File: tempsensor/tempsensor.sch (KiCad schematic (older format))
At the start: 68 parts, among them J1 USB_B_Micro, Q1 BC817, Q2 BC817, Q3 BC817, SW1 SW_DIP_x06, SW2 PW_OFF, SW3 PW_ON, U1 PCF8574, U2 ESP-12F, U3 24C16, U4 MCP73831-2-OT, U5 MCP9844, U6 MAX17620

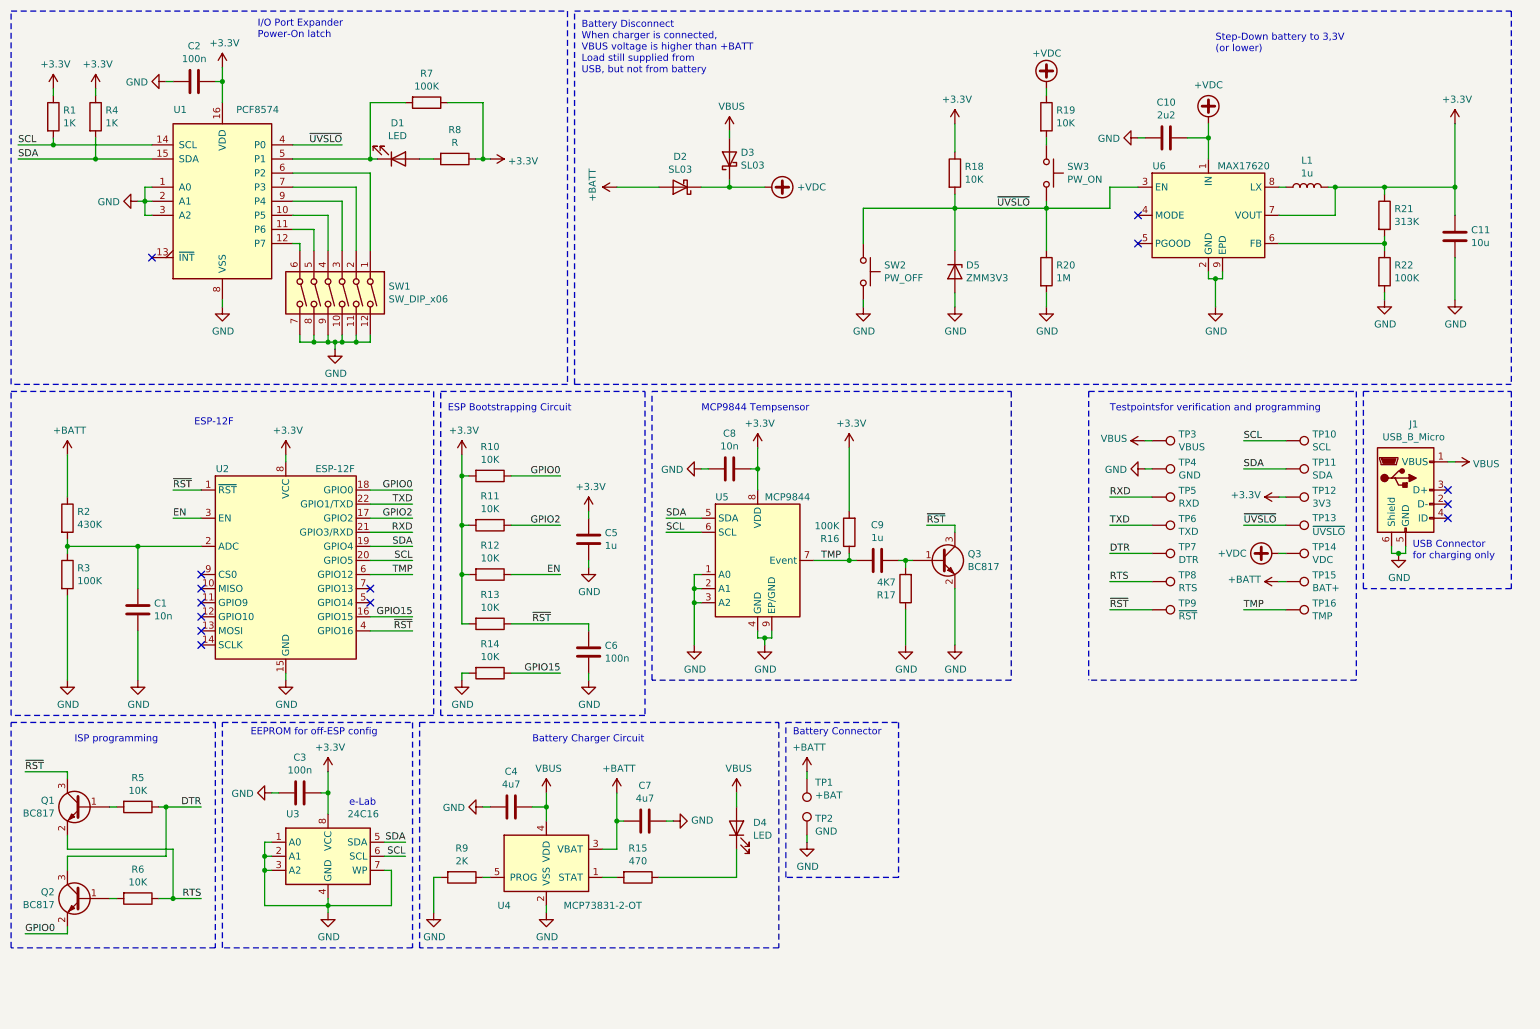
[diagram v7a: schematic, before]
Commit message: Created 4x4cm PCB for tempsensor, first routing done.
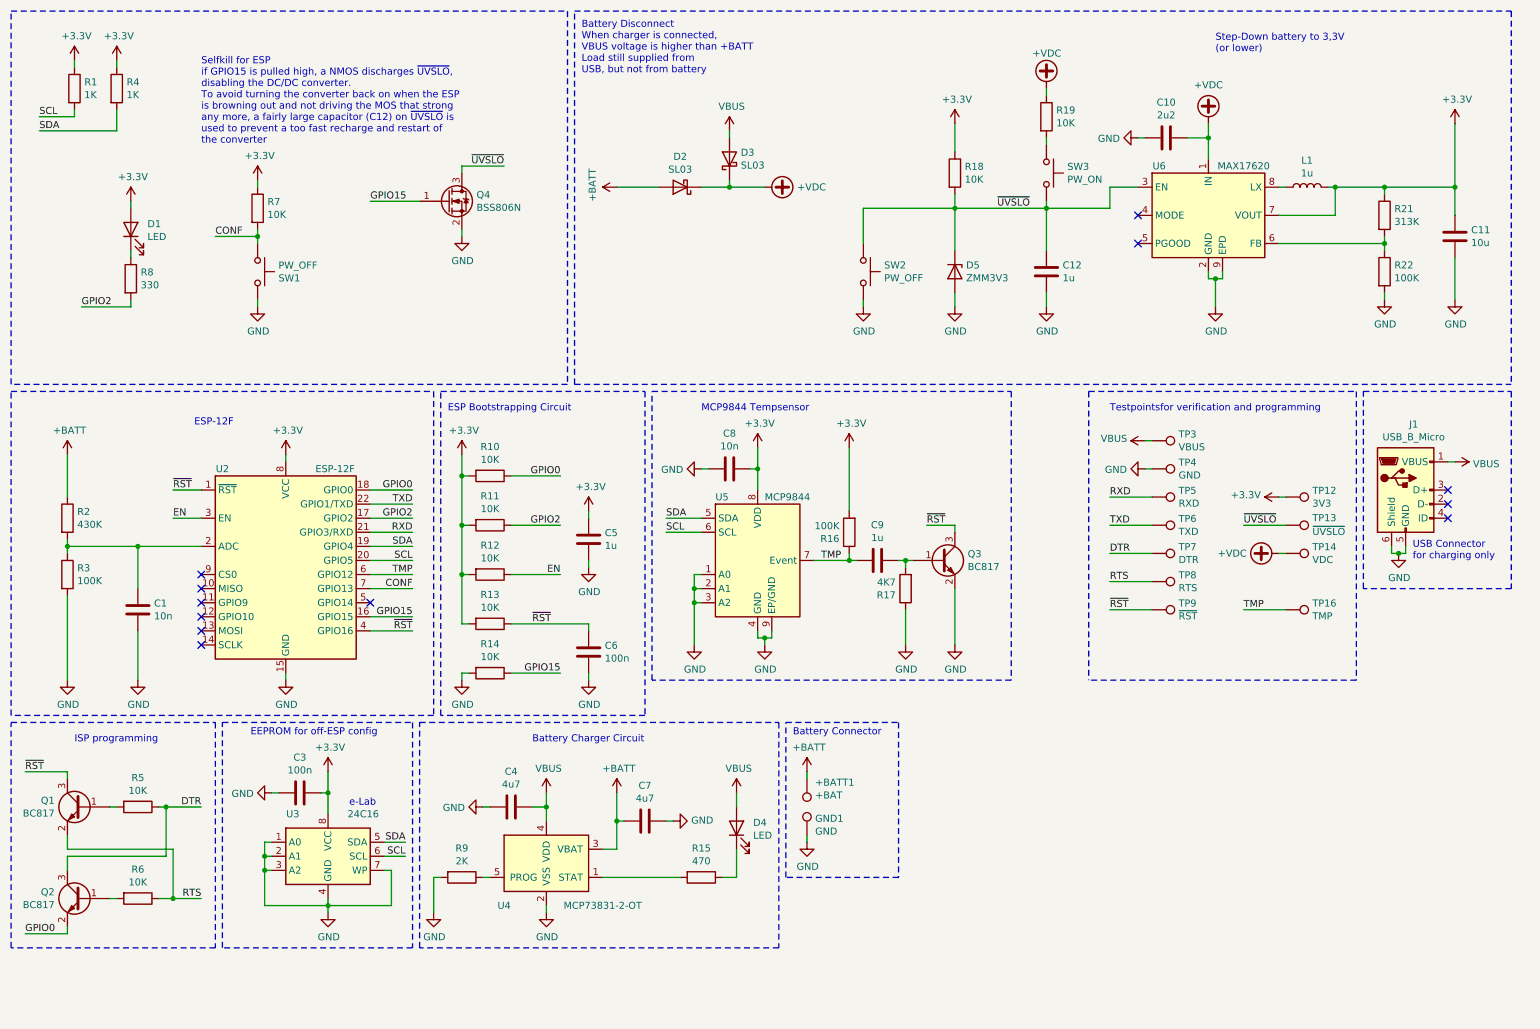
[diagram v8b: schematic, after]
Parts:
- removed C2: 100n, Capacitor_SMD:C_0603_1608Metric, symbol Device:C
- removed R20: 1M, Resistor_SMD:R_0603_1608Metric, symbol Device:R
- removed SW1: SW_DIP_x06, Button_Switch_SMD:SW_DIP_SPSTx06_Slide_Omron_A6S-610x_W8.9mm_P2.54mm, symbol Switch:SW_DIP_x06
- removed TP10: SCL, TestPoint:TestPoint_Pad_D1.0mm, symbol Connector:TestPoint
- removed TP11: SDA, TestPoint:TestPoint_Pad_D1.0mm, symbol Connector:TestPoint
- removed TP15: BAT+, TestPoint:TestPoint_Pad_D1.0mm, symbol Connector:TestPoint
- removed U1: PCF8574, Package_SO:SOIC-16W_7.5x10.3mm_P1.27mm, symbol Interface_Expansion:PCF8574
- added C12: 1u, Capacitor_SMD:C_0603_1608Metric, symbol Device:C
- added Q4: BSS806N, Package_TO_SOT_SMD:SOT-23, symbol Device:Q_NMOS_GSD
- added SW1: PW_OFF, Button_Switch_THT:SW_PUSH_6mm_H5mm, symbol Switch:SW_Push
- R7: value 100K -> 10K
- R8: value R -> 330
- renumbered TP1 to +BATT1, TP2 to GND1
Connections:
- net +3V3: now also D1.2 (A); no longer R8.1
- net GND: now also C12.2, Q4.2 (S), SW1.1
- net GPIO15: now also Q4.1 (G)
- net GPIO2: now also R8.2
- net ~UVSLO: now also C12.1, Q4.3 (D)
- net CONF: now reaches U2.7 (GPIO13)
- net CONF: now also R7.2, SW1.2
- net at D1.1 (K): now also R8.1; no longer R7.2
- no-connect marks 14 -> 12
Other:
- note added: "Selfkill for ESP\nif GPIO15 is pulled high, a NMOS discharges ~UVSLO~, \ndisabling the DC/DC converter.\nTo avoid turning the converter back on when the ESP \nis browning out and not driving the MOS that strong \nany more, a fairly large capacitor (C12) on ~UVSLO~ is \nused to prevent a too fast recharge and restart of \nthe converter"
- note removed: "I/O Port Expander\nPower-On latch"
- moved on the sheet: R1, R15, R4
